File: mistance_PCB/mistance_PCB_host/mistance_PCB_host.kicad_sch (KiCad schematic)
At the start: 81 parts, among them J3 GRPB052VWVN-RC, J4 OLED, J5 SMA-J-P-X-ST-TH1, Q1 Q_PMOS_DSG, Q2 UMH3N, U1 ESP32-WROOM-32E, U2 TPS61200DRC, U3 MCP73831-2-OT, U4 AMS1117-3.3, U5 CP2104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

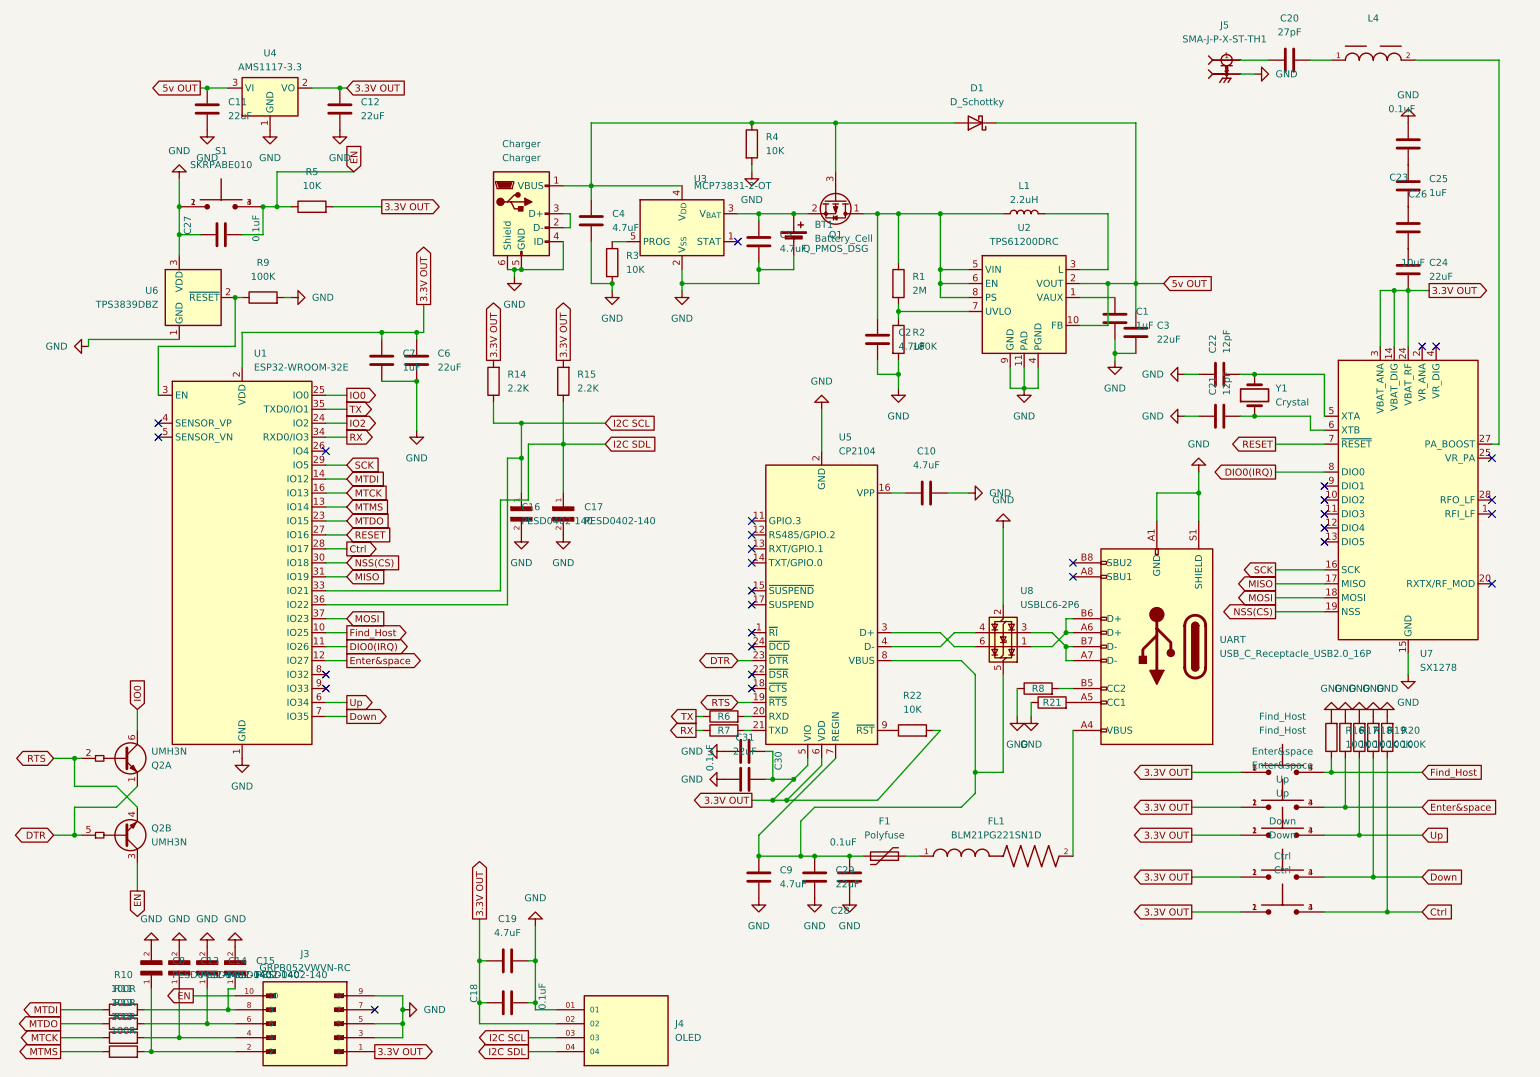
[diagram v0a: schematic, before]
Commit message: SCH finish PCB writing
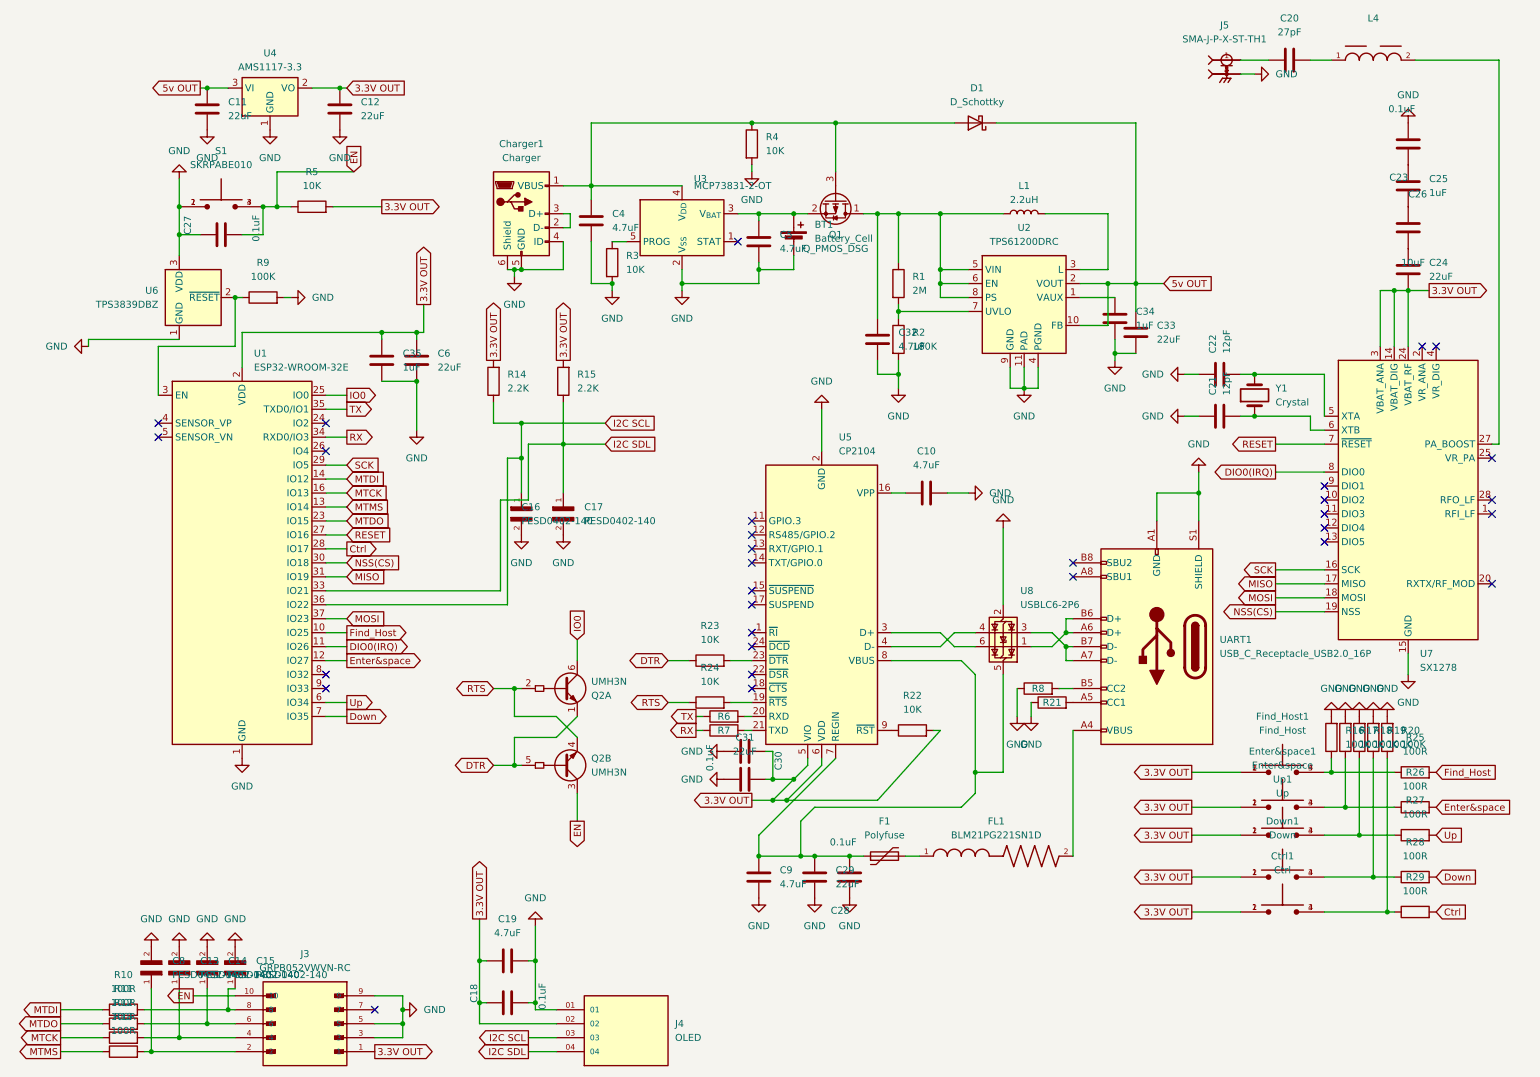
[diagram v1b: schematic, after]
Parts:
- removed C1, C7: 1uF, Capacitor_SMD:C_1210_3225Metric, symbol Device:C
- removed C2: 4.7uF, Capacitor_SMD:C_1210_3225Metric, symbol Device:C
- removed C3: 22uF, Capacitor_SMD:C_1210_3225Metric, symbol Device:C
- added C32: 4.7uF, Capacitor_SMD:C_0603_1608Metric, symbol Device:C
- added C33: 22uF, Capacitor_SMD:C_0805_2012Metric, symbol Device:C
- added C34, C35: 1uF, Capacitor_SMD:C_0603_1608Metric, symbol Device:C
- added R23, R24: 10K, Resistor_SMD:R_0603_1608Metric, symbol Device:R
- added R25, R26, R27, R28, R29: 100R, Resistor_SMD:R_0603_1608Metric, symbol Device:R
- C10, C19, C25, C26, C4, C5, C9: footprint Capacitor_SMD:C_1210_3225Metric -> Capacitor_SMD:C_0603_1608Metric
- C11, C12, C24, C29, C31, C6: footprint Capacitor_SMD:C_1210_3225Metric -> Capacitor_SMD:C_0805_2012Metric
- UART1: renamed from UART; footprint (none) -> 12402012E212A:AMPHENOL_12402012E212A
- renumbered Charger to Charger1, Ctrl to Ctrl1, Down to Down1, Enter&space to Enter&space1, Find_Host to Find_Host1, Up to Up1
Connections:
- net 3.3V OUT: now also C31.2, C35.1; no longer C31.1
- net 5v OUT: now also C33.1
- net Ctrl: now also R29.2; no longer Ctrl1.3, Ctrl1.4, R20.1
- net DTR: now also R23.1; no longer U5.23 (~{DTR})
- net Down: now also R28.2; no longer Down1.3, Down1.4, R19.1
- net Enter&space: now also R26.2; no longer Enter&space1.3, Enter&space1.4, R17.1
- net Find_Host: now also R25.2; no longer Find_Host1.3, Find_Host1.4, R16.1
- net GND: now also C29.2, C31.1, C32.2, C33.2, C34.2, C35.2; no longer C29.1, C31.2
- net RTS: now also R24.1; no longer U5.19 (~{RTS})
- net Up: now also R27.2; no longer R18.1, Up1.3, Up1.4
- net at L1.1, Q1.1 (D), R1.1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: now also C32.1
- net at C28.2, C9.1, F1.1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: now also C29.1; no longer C29.2
- net at U2.1 (VAUX): now also C34.1
- net IO2: no longer names the net of U1.24 (IO2)
- new net: Ctrl1.3, Ctrl1.4, R20.1, R29.1
- new net: R24.2, U5.19 (~{RTS})
- new net: R18.1, R27.1, Up1.3, Up1.4
- new net: R23.2, U5.23 (~{DTR})
- new net: Enter&space1.3, Enter&space1.4, R17.1, R26.1
- new net: Down1.3, Down1.4, R19.1, R28.1
- new net: Find_Host1.3, Find_Host1.4, R16.1, R25.1
- no-connect marks 30 -> 31
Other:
- moved on the sheet: Q2A, Q2B

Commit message: PCB writing
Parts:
- R21: value 22R -> 5.1K
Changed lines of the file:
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@@
 			)
 		)
-		(property "Value" "22R"
+		(property "Value" "5.1K"
 			(at 200.914 128.524 90)
 			(effects
